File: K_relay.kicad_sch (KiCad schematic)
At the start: 30 parts, among them J1 ANT3, J2 Conn_02x05_Odd_Even, J3 ANT1, J4 ANT4, J5 ANT2, J6 FROM ATU OUT, J7 TO ATU IN, J8 FROM LPF, K1 TRA2 L-12VDC-S-Z, K2 TRA2 L-12VDC-S-Z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

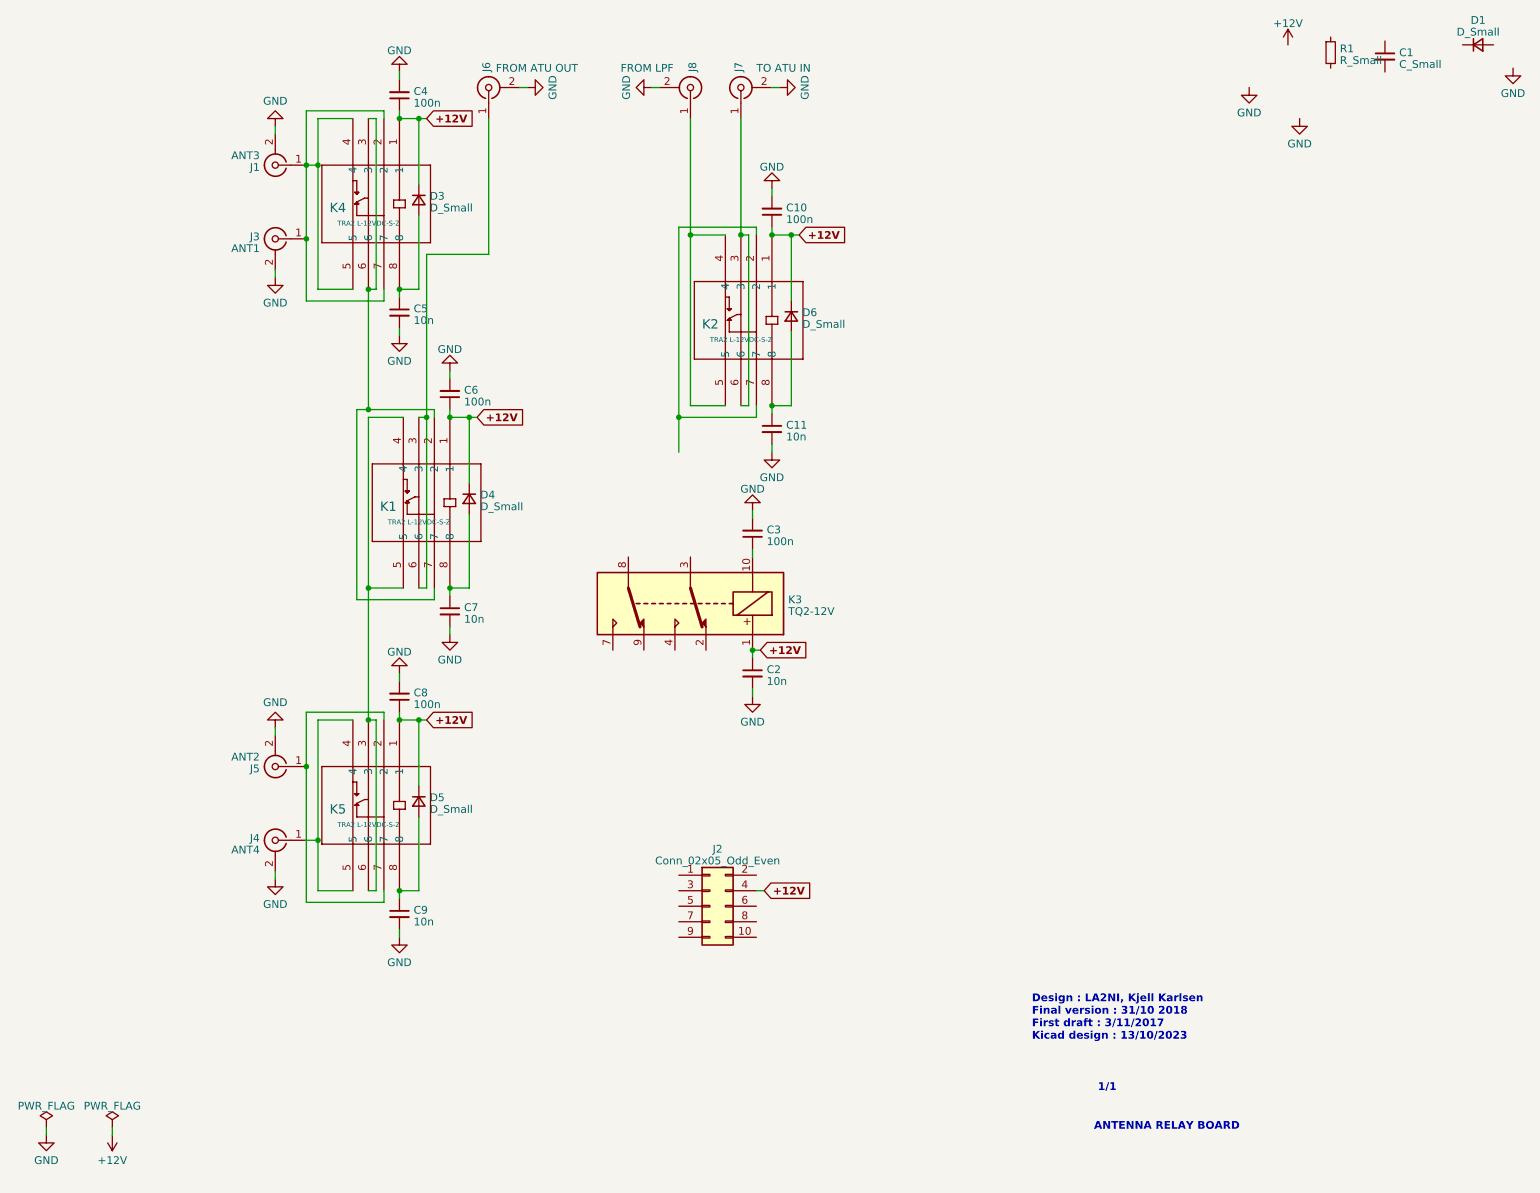
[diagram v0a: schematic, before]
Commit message: schematic completed
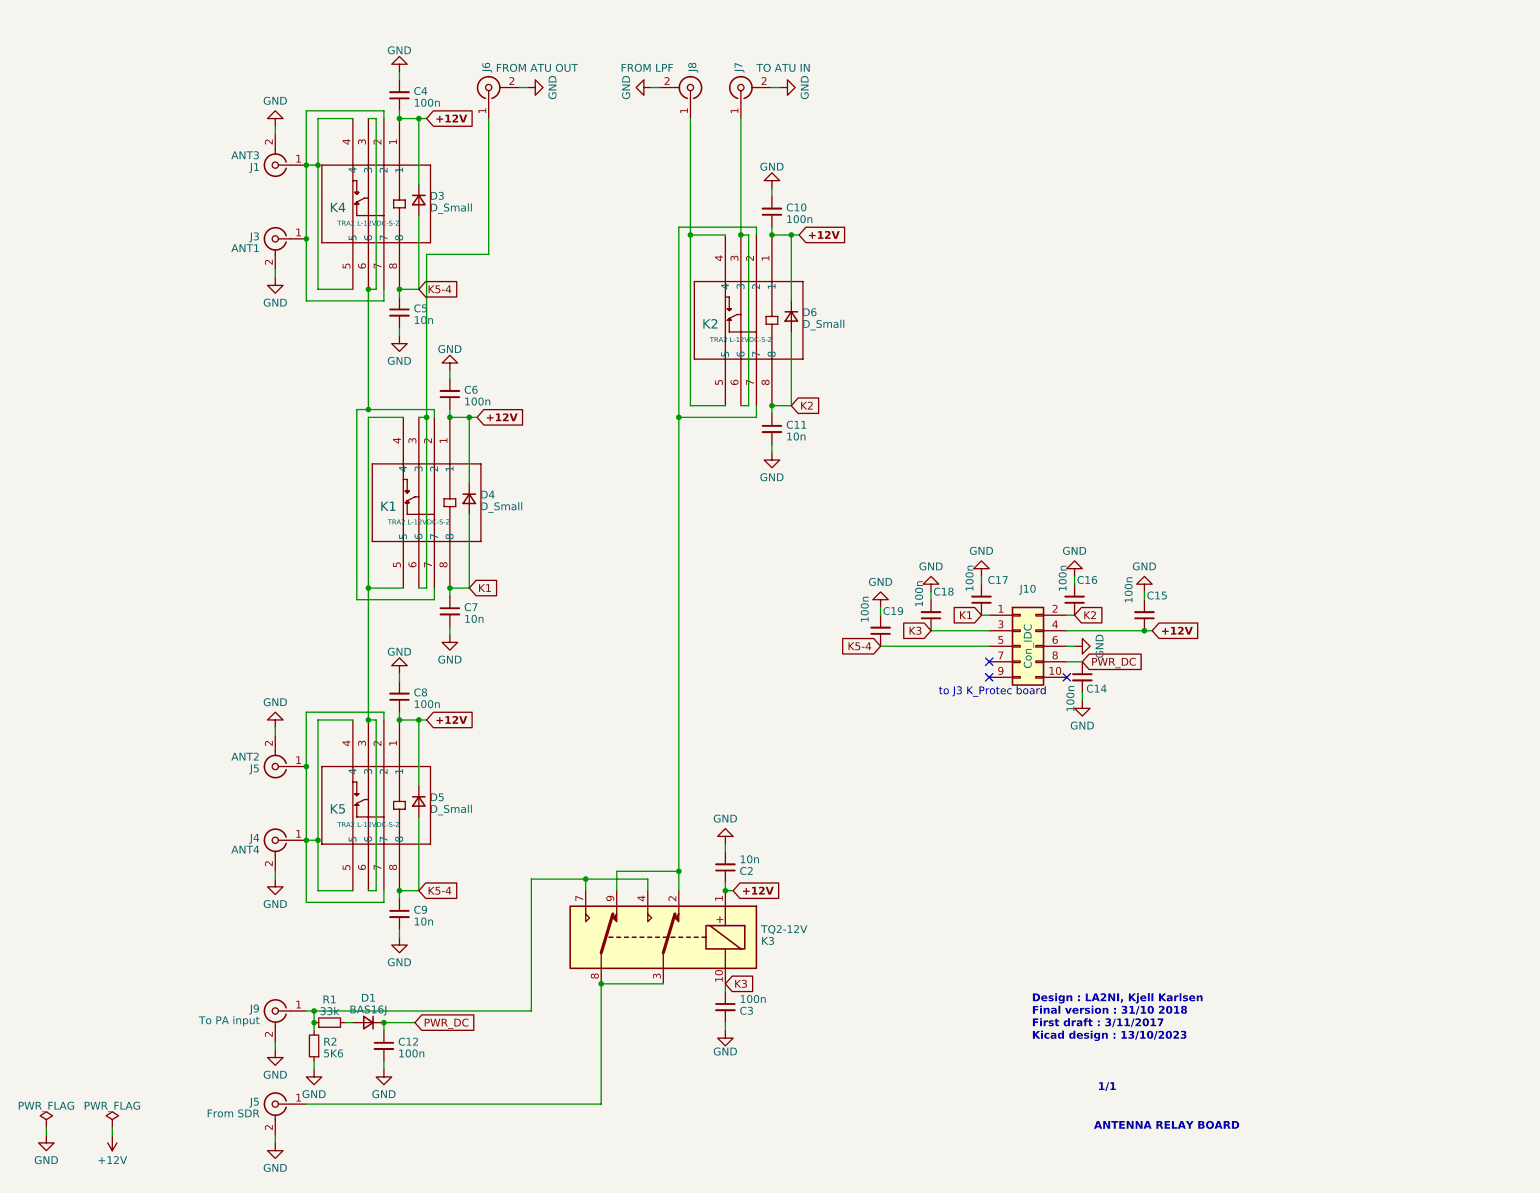
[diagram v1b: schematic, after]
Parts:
- removed C1: C_Small, symbol Device:C_Small
- added C12, C14, C15, C16, C17, C18, C19: 100n, symbol Device:C_Small
- added J5: From SDR, symbol Connector:Conn_Coaxial
- added J9: To PA input, symbol Connector:Conn_Coaxial
- added R2: 5K6, symbol Device:R_Small
- D1: value D_Small -> BAS16J
- J10: renamed from J2; value Conn_02x05_Odd_Even -> Con_IDC
- R1: value R_Small -> 33k
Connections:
- net +12V: now also C15.1
- net GND: now also J10.6 (Pin_6), C12.2, C14.2, C15.2, C16.2, C17.2, C18.2, C19.2, J5.2 (Ext), J9.2 (Ext), R2.1
- net K2: now reaches C11.1, D6.2 (A), K2.8
- net K2: now also J10.2 (Pin_2), C16.1
- net at R1.1: now also K3.4, K3.7, J9.1 (In), R2.2
- net at R1.2: now also D1.2 (A)
- net at J5.1 (In), K5.2, K5.7: now also J4.1 (In), K5.4, K5.5
- net K3: now reaches C3.1, K3.10
- net K3: now also J10.3 (Pin_3), C18.1
- net at K3.2: now also K2.2, K2.7, K3.9
- net at K3.3: now also K3.8, J5.1 (In)
- net K5-4: now reaches C5.1, D3.2 (A), K4.8
- net K5-4: now also C9.1, D5.2 (A), J10.5 (Pin_5), K5.8, C19.1
- net K1: now reaches C7.1, D4.2 (A), K1.8
- net K1: now also J10.1 (Pin_1), C17.1
- net PWR_DC: now reaches J10.8 (Pin_8)
- net PWR_DC: now also D1.1 (K), C12.1, C14.1
- no-connect marks 0 -> 3
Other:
- note added: "to J3 K_Protec board"
- moved on the sheet: C2, C3, D1, J10, K3

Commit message: schematic completed, footprint & 3D shapes ok
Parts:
- added C1, C13: 22p, Capacitor_SMD:C_0805_2012Metric_Pad1.18x1.45mm_HandSolder, symbol Device:C_Small
- added C20: 100p, Capacitor_SMD:C_0805_2012Metric_Pad1.18x1.45mm_HandSolder, symbol Device:C_Small
- added J11: To CTL, SMA_PINS:SMA_PINS, symbol Connector:Conn_Coaxial
- C12, C14, C15, C16, C17, C18, C19: footprint (none) -> Capacitor_SMD:C_0805_2012Metric_Pad1.18x1.45mm_HandSolder
- D1, D3, D4, D5, D6: footprint (none) -> Diode_SMD:D_SOD-323_HandSoldering
- J1, J4: footprint (none) -> Conn_N:Coaxial_N_Flange
- J2: renamed from J3; footprint (none) -> Conn_N:Coaxial_N_Flange
- J3: renamed from J5; footprint (none) -> Conn_N:Coaxial_N_Flange
- J5: value From SDR -> TRX From SDR; footprint (none) -> SMA_PINS:SMA_PINS
- J6, J7, J8: footprint (none) -> BNC_Amphenol_031-5329-51RFX:BNC_Amphenol_031532951RFX
- J9: footprint (none) -> SMA_PINS:SMA_PINS
- R1, R2: footprint (none) -> Resistor_SMD:R_0805_2012Metric_Pad1.20x1.40mm_HandSolder
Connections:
- net GND: now also C20.1, J11.2 (Ext)
- net at J5.1 (In), K3.3, K3.8: now also C1.1
- new net: C1.2, C13.1
- new net: C13.2, C20.2, J11.1 (In)
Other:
- note added: "(qrp/tune/qro)"
- note added: "N Flange"
- note added: "SMA Straight"
- note added: "bnc straight"

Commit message: traces completed, silk need some cleaning
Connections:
- net at J3.1 (In), K5.2, K5.7: no longer J4.1 (In), K5.4, K5.5
- net at J1.1 (In), K4.4, K4.5: no longer J2.1 (In), K4.2, K4.7
- new net: J4.1 (In), K5.4, K5.5
- new net: J2.1 (In), K4.2, K4.7
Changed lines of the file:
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@@
   (junction (at 61.595 170.815) (diameter 0) (color 0 0 0 0)
   )
-  (junction (at 60.325 32.385) (diameter 0) (color 0 0 0 0)
-  )
   (junction (at 75.565 52.705) (diameter 0) (color 0 0 0 0)
   )
@@
   )
   (junction (at 75.565 123.19) (diameter 0) (color 0 0 0 0)
-  )
-  (junction (at 60.325 142.875) (diameter 0) (color 0 0 0 0)
   )
   (junction (at 197.485 108.585) (diameter 0) (color 0 0 0 0)
@@
     (stroke (width 0) (type default))
   )
-  (wire (pts (xy 60.325 130.81) (xy 60.325 142.875))
-    (stroke (width 0) (type default))
-  )
   (wire (pts (xy 70.485 73.66) (xy 70.485 101.6))
     (stroke (width 0) (type default))
@@
     (stroke (width 0) (type default))
   )
-  (wire (pts (xy 60.325 142.875) (xy 60.325 153.035))
+  (wire (pts (xy 60.325 130.81) (xy 60.325 153.035))
     (stroke (width 0) (type default))
   )
@@
     (stroke (width 0) (type default))
   )
-  (wire (pts (xy 60.325 32.385) (xy 60.325 44.45))
-    (stroke (width 0) (type default))
-  )
   (wire (pts (xy 78.74 151.13) (xy 75.565 151.13))
     (stroke (width 0) (type default))
@@
     (stroke (width 0) (type default))
   )
-  (wire (pts (xy 60.325 23.495) (xy 60.325 32.385))
-    (stroke (width 0) (type default))
-  )
+  (wire (pts (xy 60.325 23.495) (xy 60.325 44.45))
+    (stroke (width 0) (type default))
+  )
